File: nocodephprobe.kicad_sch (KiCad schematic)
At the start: 30 parts, among them Q1 2N7002, U1 LMV358a, U2 ICL7106CPL, U3 MCP1501-10xCH, U4 VI-301-1

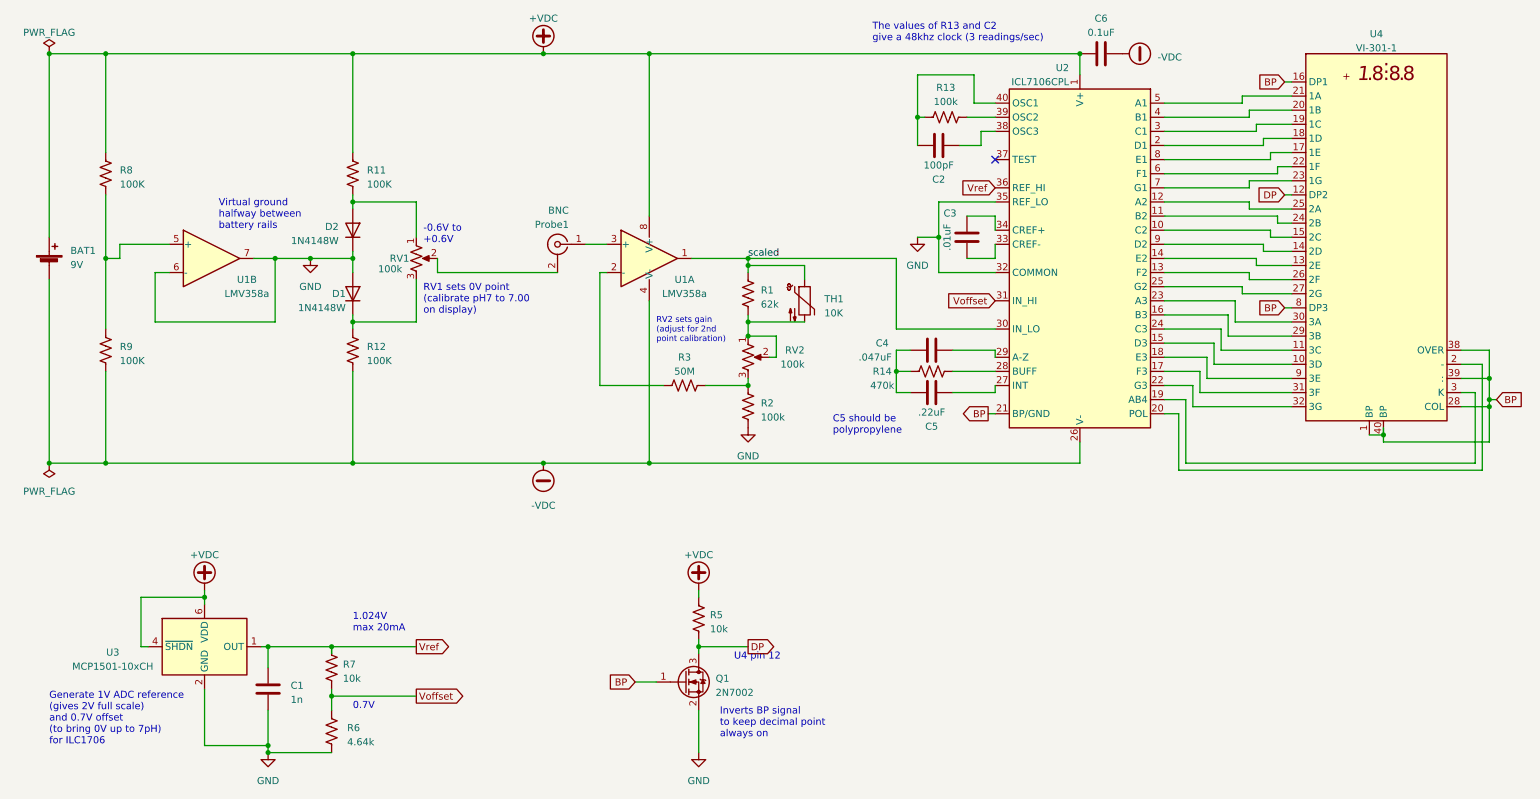
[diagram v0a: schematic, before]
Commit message: Use 10k pots instead of 100k
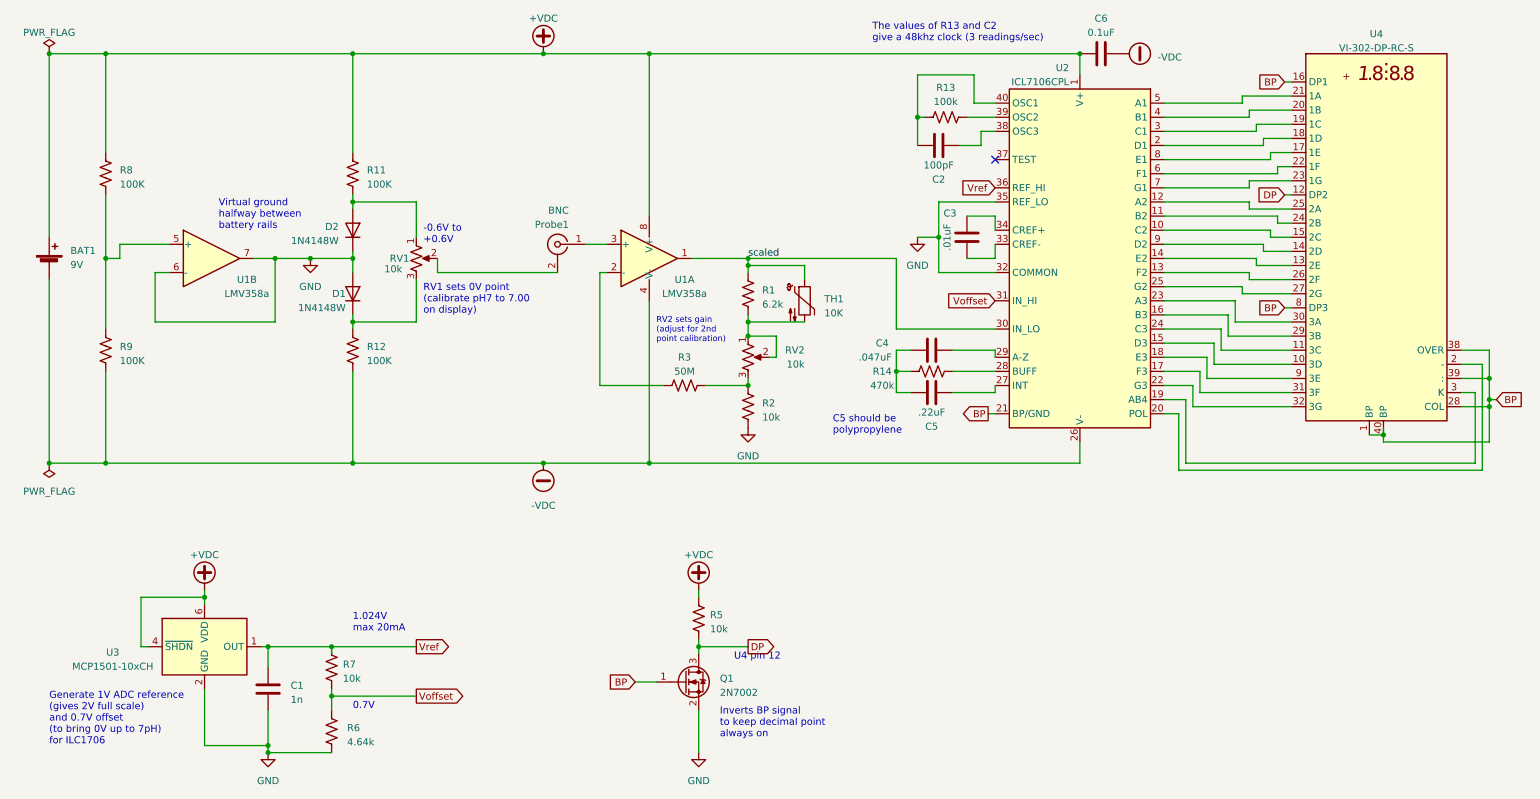
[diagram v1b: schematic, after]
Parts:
- Probe1: footprint (none) -> Connector_Coaxial:BNC_Amphenol_031-6575_Horizontal
- Q1: footprint Resistor_SMD:R_0805_2012Metric_Pad1.20x1.40mm_HandSolder -> Package_TO_SOT_SMD:SOT-23
- R1: value 62k -> 6.2k
- R2, RV1, RV2: value 100k -> 10k
- U4: value VI-301-1 -> VI-302-DP-RC-S
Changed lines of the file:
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@@
       (effects (font (size 1.27 1.27)))
     )
-    (property "Value" "VI-301-1" (at 256.54 25.654 0)
+    (property "Value" "VI-302-DP-RC-S" (at 256.54 25.654 0)
       (effects (font (size 1.27 1.27)))
     )
@@
       (effects (font (size 1.27 1.27)) hide)
     )
-    (property "Datasheet" "https://media.digikey.com/pdf/Data%20Sheets/Varitronix%20PDFs/VI-301.pdf" (at 259.08 107.95 0)
+    (property "Datasheet" "https://media.digikey.com/pdf/Data%20Sheets/Varitronix%20PDFs/VI-302%20Line%20Drawing.pdf" (at 259.08 107.95 0)
       (effects (font (size 1.27 1.27)) hide)
     )
@@
   (symbol (lib_id "Device:R_US") (at 143.51 69.85 180) (unit 1)
     (in_bom yes) (on_board yes) (dnp no) (fields_autoplaced)
-    (property "Reference" "R1" (at 145.796 69.215 0)
-      (effects (font (size 1.27 1.27)) (justify right))
-    )
-    (property "Value" "62k" (at 145.796 71.755 0)
+    (property "Reference" "R1" (at 146.05 69.215 0)
+      (effects (font (size 1.27 1.27)) (justify right))
+    )
+    (property "Value" "6.2k" (at 146.05 71.755 0)
       (effects (font (size 1.27 1.27)) (justify right))
     )
@@
     )
   )
+  (symbol (lib_id "Transistor_FET:2N7002") (at 132.08 139.7 0) (unit 1)
+    (in_bom yes) (on_board yes) (dnp no) (fields_autoplaced)
+    (property "Reference" "Q1" (at 138.43 139.065 0)
+      (effects (font (size 1.27 1.27)) (justify left))
+    )
+    (property "Value" "2N7002" (at 138.43 141.605 0)
+      (effects (font (size 1.27 1.27)) (justify left))
+    )
+    (property "Footprint" "Package_TO_SOT_SMD:SOT-23" (at 137.16 141.605 0)
+      (effects (font (size 1.27 1.27) italic) (justify left) hide)
+    )
+    (property "Datasheet" "https://www.onsemi.com/pub/Collateral/NDS7002A-D.PDF" (at 132.08 139.7 0)
+      (effects (font (size 1.27 1.27)) (justify left) hide)
+    )
+    (pin "1")
+    (pin "2")
+    (pin "3")
+    (instances
+      (project "nocodephprobe"
+        (path "/2036f74b-8ede-4e4d-84df-8cc119de9ab1"
+          (reference "Q1") (unit 1)
+        )
+      )
+    )
+  )
   (symbol (lib_id "Device:C") (at 176.53 80.01 270) (unit 1)
     (in_bom yes) (on_board yes) (dnp no)
@@
   (symbol (lib_id "Device:R_US") (at 143.51 90.17 180) (unit 1)
     (in_bom yes) (on_board yes) (dnp no) (fields_autoplaced)
-    (property "Reference" "R2" (at 145.796 89.535 0)
-      (effects (font (size 1.27 1.27)) (justify right))
-    )
-    (property "Value" "100k" (at 145.796 92.075 0)
+    (property "Reference" "R2" (at 146.05 89.535 0)
+      (effects (font (size 1.27 1.27)) (justify right))
+    )
+    (property "Value" "10k" (at 146.05 92.075 0)
       (effects (font (size 1.27 1.27)) (justify right))
     )
@@
       (effects (font (size 1.27 1.27)) (justify right))
     )
-    (property "Value" "100k" (at 153.67 82.55 0)
+    (property "Value" "10k" (at 153.67 82.55 0)
       (effects (font (size 1.27 1.27)) (justify right))
     )
@@
       (effects (font (size 1.27 1.27)) (justify right))
     )
-    (property "Value" "100k" (at 81.28 65.405 0)
+    (property "Value" "10k" (at 81.28 65.405 0)
       (effects (font (size 1.27 1.27)) (justify right))
     )
@@
     )
   )
-  (symbol (lib_id "Transistor_FET:2N7002") (at 132.08 139.7 0) (unit 1)
-    (in_bom yes) (on_board yes) (dnp no) (fields_autoplaced)
-    (property "Reference" "Q1" (at 137.668 139.065 0)
-      (effects (font (size 1.27 1.27)) (justify left))
-    )
-    (property "Value" "2N7002" (at 137.668 141.605 0)
-      (effects (font (size 1.27 1.27)) (justify left))
-    )
-    (property "Footprint" "Resistor_SMD:R_0805_2012Metric_Pad1.20x1.40mm_HandSolder" (at 137.16 141.605 0)
-      (effects (font (size 1.27 1.27) italic) (justify left) hide)
-    )
-    (property "Datasheet" "https://www.onsemi.com/pub/Collateral/NDS7002A-D.PDF" (at 132.08 139.7 0)
-      (effects (font (size 1.27 1.27)) (justify left) hide)
-    )
-    (pin "1")
-    (pin "2")
-    (pin "3")
-    (instances
-      (project "nocodephprobe"
-        (path "/2036f74b-8ede-4e4d-84df-8cc119de9ab1"
-          (reference "Q1") (unit 1)
-        )
-      )
-    )
-  )
   (symbol (lib_id "Device:R_US") (at 27.94 48.26 180) (unit 1)
     (in_bom yes) (on_board yes) (dnp no) (fields_autoplaced)
@@
       (effects (font (size 1.27 1.27)) (justify left))
     )
-    (property "Footprint" "" (at 109.22 60.96 0)
-      (effects (font (size 1.27 1.27)) hide)
-    )
+    (property "Footprint" "Connector_Coaxial:BNC_Amphenol_031-6575_Horizontal" (at 109.22 60.96 0)
+      (effects (font (size 1.27 1.27)) hide)
+    )

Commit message: Use only 1 diode in offset circuit
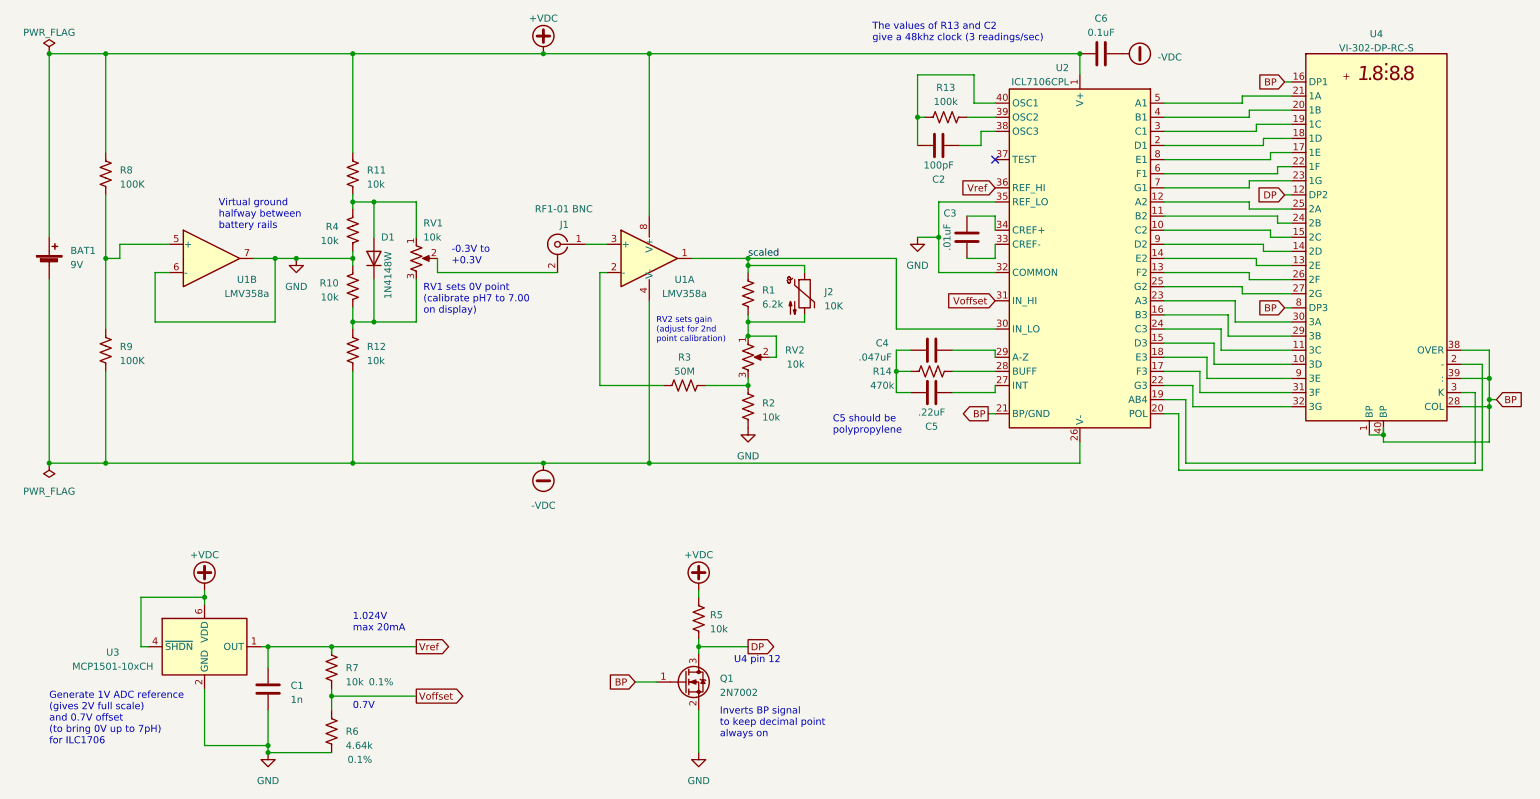
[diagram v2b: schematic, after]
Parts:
- removed D2: 1N4148W, Diode_SMD:D_SOD-123, symbol Diode:1N4148W
- added R10, R4: 10k, Resistor_SMD:R_0805_2012Metric_Pad1.20x1.40mm_HandSolder, symbol Device:R_US
- C5: Material (none) -> film (polypropylene); Type film/polypropylene -> (none)
- J1: renamed from Probe1; value BNC -> RF1-01 BNC; digikey (none) -> 2057-RF1-01K-D-00-50-BK-HDW-ND
- J2: renamed from TH1; footprint Connector_Audio:Jack_3.5mm_CUI_SJ1-3533NG_Horizontal_CircularHoles -> STX-3120-3B:KYCON_STX-3120-3B
- R11, R12: value 100K -> 10k
- R6, R7: Tolerance (none) -> 0.1%
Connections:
- net GND: now also R10.2, R4.1; no longer D1.2 (A)
- net at R11.1, RV1.1: now also D1.2 (A), R4.2
- net at R1.1, RV2.1, RV2.2: now also J2.5; no longer J2.2
- net at D1.1 (K), R12.2, RV1.3: now also R10.1
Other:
- note added: "-0.3V to +0.3V"
- note removed: "-0.6V to +0.6V"
- moved on the sheet: D1, J2

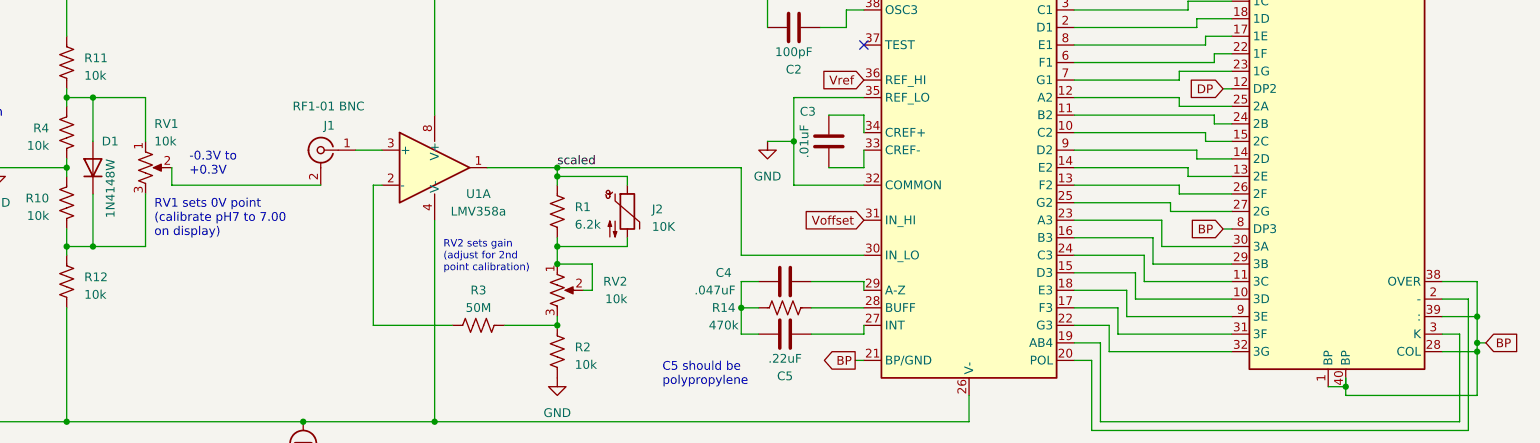
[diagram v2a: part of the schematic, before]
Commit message: Add header footprints to bat and pots
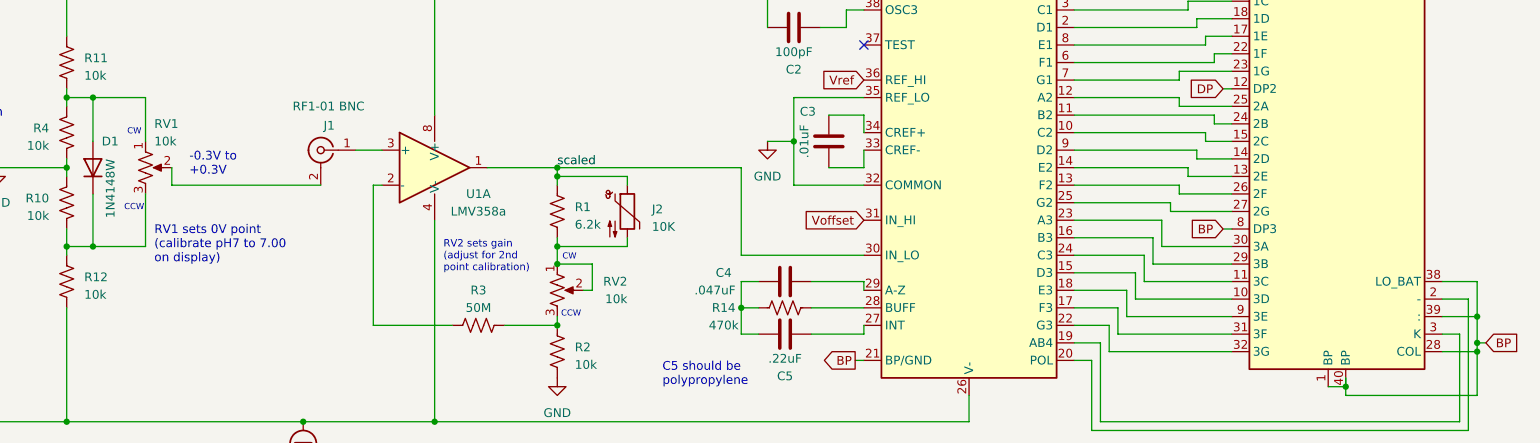
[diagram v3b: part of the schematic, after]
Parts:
- BAT1: footprint Connector_Wire:SolderWire-0.75sqmm_1x02_P4.8mm_D1.25mm_OD2.3mm_Relief -> Connector_Molex:Molex_KK-396_A-41792-0002_1x02_P3.96mm_Horizontal
- RV1, RV2: footprint Connector_Wire:SolderWire-0.75sqmm_1x03_P7mm_D1.25mm_OD3.5mm -> Connector_PinHeader_2.54mm:PinHeader_1x03_P2.54mm_Horizontal
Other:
- note added: "CCW"
- note added: "CW"
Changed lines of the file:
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@@
     (stroke (width 0) (type default))
+  )
+  (text "CCW" (at 80.7224 69.8624 0)
+    (effects (font (size 0.889 0.889)) (justify left bottom))
   )
   (text "C5 should be\npolypropylene" (at 158.75 95.25 0)
@@
   )
   (text "RV1 sets 0V point\n(calibrate pH7 to 7.00\non display)"
-    (at 85.09 73.66 0)
+    (at 85.09 77.47 0)
     (effects (font (size 1.27 1.27)) (justify left bottom))
   )
@@
     (effects (font (size 1.27 1.27)) (justify left bottom))
   )
+  (text "CCW" (at 144.0557 85.2966 0)
+    (effects (font (size 0.889 0.889)) (justify left bottom))
+  )
   (text "U4 pin 12" (at 140.97 136.525 0)
     (effects (font (size 1.27 1.27)) (justify left bottom))
@@
   (text "0.7V" (at 72.39 144.78 0)
     (effects (font (size 1.27 1.27)) (justify left bottom))
+  )
+  (text "CW" (at 144.2493 77.0231 0)
+    (effects (font (size 0.889 0.889)) (justify left bottom))
+  )
+  (text "CW" (at 81.1698 58.8836 0)
+    (effects (font (size 0.889 0.889)) (justify left bottom))
   )
   (text "Inverts BP signal\nto keep decimal point\nalways on" (at 138.43 149.86 0)
@@
       (effects (font (size 1.27 1.27)) (justify right))
     )
-    (property "Footprint" "Connector_Wire:SolderWire-0.75sqmm_1x03_P7mm_D1.25mm_OD3.5mm" (at 143.51 81.28 0)
+    (property "Footprint" "Connector_PinHeader_2.54mm:PinHeader_1x03_P2.54mm_Horizontal" (at 143.51 81.28 0)
       (effects (font (size 1.27 1.27)) hide)
     )
@@
       (effects (font (size 1.27 1.27)) (justify left))
     )
-    (property "Footprint" "Connector_Wire:SolderWire-0.75sqmm_1x02_P4.8mm_D1.25mm_OD2.3mm_Relief" (at 17.78 63.246 90)
+    (property "Footprint" "Connector_Molex:Molex_KK-396_A-41792-0002_1x02_P3.96mm_Horizontal" (at 17.78 63.246 90)
       (effects (font (size 1.27 1.27)) hide)
     )
@@
       (effects (font (size 1.27 1.27)) (justify left))
     )
-    (property "Footprint" "Connector_Wire:SolderWire-0.75sqmm_1x03_P7mm_D1.25mm_OD3.5mm" (at 83.82 63.5 0)
-      (effects (font (size 1.27 1.27)) hide)
-    )
+    (property "Footprint" "Connector_PinHeader_2.54mm:PinHeader_1x03_P2.54mm_Horizontal" (at 83.82 63.5 0)
+      (effects (font (size 1.27 1.27)) hide)
+    )
